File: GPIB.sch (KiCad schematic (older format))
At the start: 24 parts, among them P1 CONN_6, P2 CONN_2, P3 CONN_8, P4 CONN_CENTRONICS_24, SW1 SW_RESET, SW2 SW_BOOTL, U5 STM32F072CBT6, U6 SN75160B, U7 SN75162B

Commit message: Start routing
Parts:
- C10, C11, C6, C7, C8, C9: footprint (none) -> Capacitors_SMD:C_0603_HandSoldering
- D2, D3, D4: footprint (none) -> LEDs:LED-0603
- JP1, P2: footprint (none) -> Pin_Headers:Pin_Header_Straight_1x02
- P1: footprint (none) -> Pin_Headers:Pin_Header_Straight_1x06
- P3: footprint (none) -> Pin_Headers:Pin_Header_Straight_1x08
- P4: footprint (none) -> gpib_conn_male:gpib_conn_male
- R5, R6, R7, R8, R9: footprint (none) -> Resistors_SMD:R_0603_HandSoldering
- SW1, SW2: footprint (none) -> open-project:SW_PUSH_SMD
- U5: footprint LQFP48 -> LQFP:LQFP-48_7x7mm_Pitch0.5mm
- U6: footprint MODULE -> Housings_SOIC:SOIC-20_7.5x12.8mm_Pitch1.27mm
- U7: footprint MODULE -> Housings_SOIC:SOIC-24_7.5x15.4mm_Pitch1.27mm
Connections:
- net GND: now also P4.12 (SHIELD)

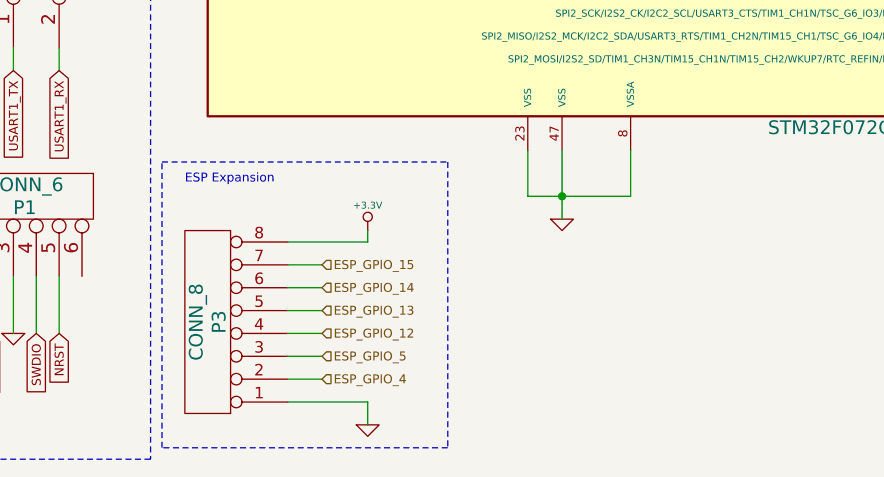
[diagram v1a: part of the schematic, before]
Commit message: Need to swap gpib line driver buses on stm32
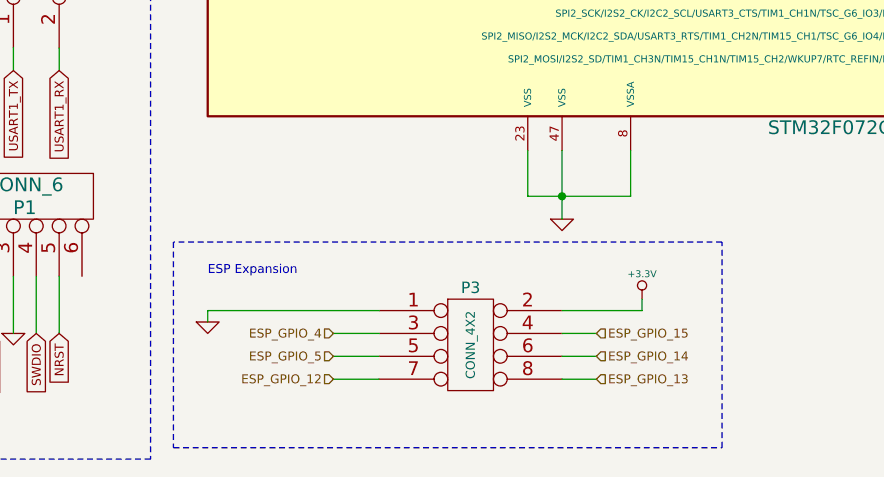
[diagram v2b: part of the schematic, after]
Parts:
- removed P3: CONN_8, Pin_Headers:Pin_Header_Straight_1x08, symbol CONN_8
- added P3: CONN_4X2, Pin_Headers:Pin_Header_Straight_2x04, symbol CONN_4X2
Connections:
- net +3.3V: now also P3.2
- net ESP_GPIO_12: now also P3.7
- net ESP_GPIO_13: now also P3.8
- net ESP_GPIO_14: now also P3.6
- net ESP_GPIO_15: now also P3.4
- net ESP_GPIO_4: now also P3.3
- net ESP_GPIO_5: now also P3.5
- net GND: now also P3.1
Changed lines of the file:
@@
 $EndComp
 $Comp
-L +3.3V #PWR44
+L +3.3V #PWR030
 U 1 1 5567B18B
 P 7200 1550
-F 0 "#PWR44" H 7200 1510 30  0001 C CNN
+F 0 "#PWR030" H 7200 1510 30  0001 C CNN
 F 1 "+3.3V" H 7200 1660 30  0000 C CNN
 F 2 "" H 7200 1550 60  0000 C CNN
@@
 	7750 3000 7750 2500
 $Comp
-L +5V #PWR48
+L +5V #PWR031
 U 1 1 5567BD37
 P 7750 2500
-F 0 "#PWR48" H 7750 2590 20  0001 C CNN
+F 0 "#PWR031" H 7750 2590 20  0001 C CNN
 F 1 "+5V" H 7750 2590 30  0000 C CNN
 F 2 "" H 7750 2500 60  0000 C CNN
@@
 $EndComp
 $Comp
-L +5V #PWR49
+L +5V #PWR032
 U 1 1 5567BE69
 P 7750 4150
-F 0 "#PWR49" H 7750 4240 20  0001 C CNN
+F 0 "#PWR032" H 7750 4240 20  0001 C CNN
 F 1 "+5V" H 7750 4240 30  0000 C CNN
 F 2 "" H 7750 4150 60  0000 C CNN
@@
 	9400 3900 9400 4050
 $Comp
-L GND #PWR52
+L GND #PWR033
 U 1 1 5567BFB4
 P 9400 4050
-F 0 "#PWR52" H 9400 4050 30  0001 C CNN
+F 0 "#PWR033" H 9400 4050 30  0001 C CNN
 F 1 "GND" H 9400 3980 30  0001 C CNN
 F 2 "" H 9400 4050 60  0000 C CNN
@@
 $EndComp
 $Comp
-L GND #PWR50
+L GND #PWR034
 U 1 1 5567BFE0
 P 9250 5900
-F 0 "#PWR50" H 9250 5900 30  0001 C CNN
+F 0 "#PWR034" H 9250 5900 30  0001 C CNN
 F 1 "GND" H 9250 5830 30  0001 C CNN
 F 2 "" H 9250 5900 60  0000 C CNN
@@
 Connection ~ 10750 1650
 $Comp
-L GND #PWR53
+L GND #PWR035
 U 1 1 5567D3C6
 P 10750 1950
-F 0 "#PWR53" H 10750 1950 30  0001 C CNN
+F 0 "#PWR035" H 10750 1950 30  0001 C CNN
 F 1 "GND" H 10750 1880 30  0001 C CNN
 F 2 "" H 10750 1950 60  0000 C CNN
@@
 Connection ~ 9300 1850
 $Comp
-L GND #PWR51
+L GND #PWR036
 U 1 1 5567D5D2
 P 9300 1950
-F 0 "#PWR51" H 9300 1950 30  0001 C CNN
+F 0 "#PWR036" H 9300 1950 30  0001 C CNN
 F 1 "GND" H 9300 1880 30  0001 C CNN
 F 2 "" H 9300 1950 60  0000 C CNN
@@
 	9250 4750 9400 4750
 $Comp
-L GND #PWR47
+L GND #PWR037
 U 1 1 556803AF
 P 7500 4600
-F 0 "#PWR47" H 7500 4600 30  0001 C CNN
+F 0 "#PWR037" H 7500 4600 30  0001 C CNN
 F 1 "GND" H 7500 4530 30  0001 C CNN
 F 2 "" H 7500 4600 60  0000 C CNN
@@
 $EndComp
 $Comp
-L GND #PWR46
+L GND #PWR038
 U 1 1 55680412
 P 7500 2950
-F 0 "#PWR46" H 7500 2950 30  0001 C CNN
+F 0 "#PWR038" H 7500 2950 30  0001 C CNN
 F 1 "GND" H 7500 2880 30  0001 C CNN
 F 2 "" H 7500 2950 60  0000 C CNN
@@
 	7500 4150 7750 4150
 $Comp
-L GND #PWR45
+L GND #PWR039
 U 1 1 5569A4CE
 P 7200 1900
-F 0 "#PWR45" H 7200 1900 30  0001 C CNN
+F 0 "#PWR039" H 7200 1900 30  0001 C CNN
 F 1 "GND" H 7200 1830 30  0001 C CNN
 F 2 "" H 7200 1900 60  0000 C CNN
@@
 	5700 1850 5500 1850
 $Comp
-L +3.3V #PWR29
+L +3.3V #PWR040
 U 1 1 5569A6B6
 P 1100 900
-F 0 "#PWR29" H 1100 860 30  0001 C CNN
+F 0 "#PWR040" H 1100 860 30  0001 C CNN
 F 1 "+3.3V" H 1100 1010 30  0000 C CNN
 F 2 "" H 1100 900 60  0000 C CNN
@@
 $EndComp
 $Comp
-L GND #PWR34
+L GND #PWR041
 U 1 1 5569A6D7
 P 1800 1500
-F 0 "#PWR34" H 1800 1500 30  0001 C CNN
+F 0 "#PWR041" H 1800 1500 30  0001 C CNN
 F 1 "GND" H 1800 1430 30  0001 C CNN
 F 2 "" H 1800 1500 60  0000 C CNN
@@
 $EndComp
 $Comp
-L +3.3V #PWR31
+L +3.3V #PWR042
 U 1 1 5569BF9D
 P 1300 2700
-F 0 "#PWR31" H 1300 2660 30  0001 C CNN
+F 0 "#PWR042" H 1300 2660 30  0001 C CNN
 F 1 "+3.3V" H 1300 2810 30  0000 C CNN
 F 2 "" H 1300 2700 60  0000 C CNN
@@
 Wire Wire Line
 	1300 3200 1850 3200
-Text HLabel 2500 7350 2    39   Input ~ 0
+Text HLabel 2550 7150 0    39   Input ~ 0
 ESP_GPIO_4
-Text HLabel 2500 7250 2    39   Input ~ 0
+Text HLabel 2550 7250 0    39   Input ~ 0
 ESP_GPIO_5
 Wire Wire Line
@@
 $EndComp
 $Comp
-L +3.3V #PWR38
+L +3.3V #PWR043
 U 1 1 556A233C
 P 3000 1350
-F 0 "#PWR38" H 3000 1310 30  0001 C CNN
+F 0 "#PWR043" H 3000 1310 30  0001 C CNN
 F 1 "+3.3V" H 3000 1460 30  0000 C CNN
 F 2 "" H 3000 1350 60  0000 C CNN
@@
 	3000 1450 3000 1350
 $Comp
-L GND #PWR35
+L GND #PWR044
 U 1 1 556A24E8
 P 2300 2000
-F 0 "#PWR35" H 2300 2000 30  0001 C CNN
+F 0 "#PWR044" H 2300 2000 30  0001 C CNN
 F 1 "GND" H 2300 1930 30  0001 C CNN
 F 2 "" H 2300 2000 60  0000 C CNN
@@
 Bootloader mode button
 $Comp
-L +3.3V #PWR39
+L +3.3V #PWR045
 U 1 1 556A2965
 P 3550 2000
-F 0 "#PWR39" H 3550 1960 30  0001 C CNN
+F 0 "#PWR045" H 3550 1960 30  0001 C CNN
 F 1 "+3.3V" H 3550 2110 30  0000 C CNN
 F 2 "" H 3550 2000 60  0000 C CNN
@@
 Connection ~ 3550 2150
 $Comp
-L +3.3V #PWR41
+L +3.3V #PWR046
 U 1 1 556A2C71
 P 5550 6200
-F 0 "#PWR41" H 5550 6160 30  0001 C CNN
+F 0 "#PWR046" H 5550 6160 30  0001 C CNN
 F 1 "+3.3V" H 5550 6310 30  0000 C CNN
 F 2 "" H 5550 6200 60  0000 C CNN
@@
 $EndComp
 $Comp
-L GND #PWR42
+L GND #PWR047
 U 1 1 556A2E45
 P 5550 6700
-F 0 "#PWR42" H 5550 6700 30  0001 C CNN
+F 0 "#PWR047" H 5550 6700 30  0001 C CNN
 F 1 "GND" H 5550 6630 30  0001 C CNN
 F 2 "" H 5550 6700 60  0000 C CNN
@@
 Connection ~ 5800 6200
 $Comp
-L GND #PWR40
+L GND #PWR048
 U 1 1 556A335E
 P 3550 6650
-F 0 "#PWR40" H 3550 6650 30  0001 C CNN
+F 0 "#PWR048" H 3550 6650 30  0001 C CNN
 F 1 "GND" H 3550 6580 30  0001 C CNN
 F 2 "" H 3550 6650 60  0000 C CNN
@@
 	5250 3750 5400 3750
 $Comp
-L GND #PWR30
+L GND #PWR049
 U 1 1 556A686C
 P 1150 7150
-F 0 "#PWR30" H 1150 7150 30  0001 C CNN
+F 0 "#PWR049" H 1150 7150 30  0001 C CNN
 F 1 "GND" H 1150 7080 30  0001 C CNN
 F 2 "" H 1150 7150 60  0000 C CNN
@@
 $EndComp
 $Comp
-L +3.3V #PWR28
+L +3.3V #PWR050
 U 1 1 556A68A8
 P 950 7150
-F 0 "#PWR28" H 950 7110 30  0001 C CNN
+F 0 "#PWR050" H 950 7110 30  0001 C CNN
 F 1 "+3.3V" H 950 7260 30  0000 C CNN
 F 2 "" H 950 7150 60  0000 C CNN
@@
 $EndComp
 $Comp
-L GND #PWR43
+L GND #PWR051
 U 1 1 556AE58B
 P 7200 1250
-F 0 "#PWR43" H 7200 1250 30  0001 C CNN
+F 0 "#PWR051" H 7200 1250 30  0001 C CNN
 F 1 "GND" H 7200 1180 30  0001 C CNN
 F 2 "" H 7200 1250 60  0000 C CNN
@@
 Wire Wire Line
 	5250 5750 5500 5750
-Text HLabel 2500 7150 2    39   Input ~ 0
+Text HLabel 2550 7350 0    39   Input ~ 0
 ESP_GPIO_12
-Text HLabel 2500 7050 2    39   Input ~ 0
+Text HLabel 3700 7350 2    39   Input ~ 0
 ESP_GPIO_13
-Text HLabel 2500 6950 2    39   Input ~ 0
+Text HLabel 3700 7250 2    39   Input ~ 0
 ESP_GPIO_14
-Text HLabel 2500 6850 2    39   Input ~ 0
+Text HLabel 3700 7150 2    39   Input ~ 0
 ESP_GPIO_15
 Text HLabel 5550 5450 2    39   Input ~ 0
@@
 	1850 4750 1700 4750
 $Comp
-L GND #PWR32
+L GND #PWR052
 U 1 1 556BAB4A
 P 1400 4800
-F 0 "#PWR32" H 1400 4800 30  0001 C CNN
+F 0 "#PWR052" H 1400 4800 30  0001 C CNN
 F 1 "GND" H 1400 4730 30  0001 C CNN
 F 2 "" H 1400 4800 60  0000 C CNN
@@
 $EndComp
 $Comp
-L +3.3V #PWR33
+L +3.3V #PWR053
 U 1 1 556BADA7
 P 1700 4750
-F 0 "#PWR33" H 1700 4710 30  0001 C CNN
+F 0 "#PWR053" H 1700 4710 30  0001 C CNN
 F 1 "+3.3V" H 1700 4860 30  0000 C CNN
 F 2 "" H 1700 4750 60  0000 C CNN
@@
 Wire Wire Line
 	1400 4650 1400 4800
-$Comp
-L CONN_8 P3
-U 1 1 556BB559
+Wire Wire Line
+	2550 7350 2750 7350
+Wire Wire Line
+	3550 7350 3700 7350
+Wire Wire Line
+	3550 7250 3700 7250
+Wire Wire Line
+	3550 7150 3700 7150
+$Comp
+L GND #PWR054
+U 1 1 556BBE46
 P 2000 7100
-F 0 "P3" V 1950 7100 60  0000 C CNN
-F 1 "CONN_8" V 2050 7100 60  0000 C CNN
-F 2 "Pin_Headers:Pin_Header_Straight_1x08" H 2000 7100 60  0001 C CNN
+F 0 "#PWR054" H 2000 7100 30  0001 C CNN
+F 1 "GND" H 2000 7030 30  0001 C CNN
+F 2 "" H 2000 7100 60  0000 C CNN
 F 3 "" H 2000 7100 60  0000 C CNN
 	1    2000 7100
-	-1   0    0    1
-$EndComp
-Wire Wire Line
-	2350 7450 2700 7450
-Wire Wire Line
-	2350 7350 2500 7350
-Wire Wire Line
-	2350 7250 2500 7250
-Wire Wire Line
-	2350 7150 2500 7150
-Wire Wire Line
-	2350 7050 2500 7050
-Wire Wire Line
-	2350 6950 2500 6950
-Wire Wire Line
-	2350 6850 2500 6850
-$Comp
-L GND #PWR37
-U 1 1 556BBE46
-P 2700 7550
-F 0 "#PWR37" H 2700 7550 30  0001 C CNN
-F 1 "GND" H 2700 7480 30  0001 C CNN
-F 2 "" H 2700 7550 60  0000 C CNN
-F 3 "" H 2700 7550 60  0000 C CNN
-	1    2700 7550
-	1    0    0    -1
-$EndComp
-$Comp
-L +3.3V #PWR36
+	1    0    0    -1
+$EndComp
+$Comp
+L +3.3V #PWR055
 U 1 1 556BBE7F
-P 2700 6700
-F 0 "#PWR36" H 2700 6660 30  0001 C CNN
-F 1 "+3.3V" H 2700 6810 30  0000 C CNN
-F 2 "" H 2700 6700 60  0000 C CNN
-F 3 "" H 2700 6700 60  0000 C CNN
-	1    2700 6700
-	1    0    0    -1
-$EndComp
-Wire Wire Line
-	2350 6750 2700 6750
-Wire Wire Line
-	2700 6750 2700 6700
-Wire Wire Line
-	2700 7450 2700 7550
-Wire Notes Line
-	1800 6400 3050 6400
-Wire Notes Line
-	3050 6400 3050 7650
-Wire Notes Line
-	3050 7650 1800 7650
-Wire Notes Line
-	1800 7650 1800 6400
-Text Notes 1900 6500 0    39   ~ 0
+P 3900 7000
+F 0 "#PWR055" H 3900 6960 30  0001 C CNN
+F 1 "+3.3V" H 3900 7110 30  0000 C CNN
+F 2 "" H 3900 7000 60  0000 C CNN
+F 3 "" H 3900 7000 60  0000 C CNN
+	1    3900 7000
+	1    0    0    -1
+$EndComp
+Wire Wire Line
+	3550 7050 3900 7050
+Wire Wire Line
+	3900 7050 3900 7000
+Text Notes 2000 6900 0    39   ~ 0
 ESP Expansion\n
 Text GLabel 1350 7150 3    39   Input ~ 0
@@
 Wire Wire Line
 	11150 1250 11150 1650
+$Comp
+L CONN_4X2 P3
+U 1 1 556C4C30
+P 3150 7200
+F 0 "P3" H 3150 7450 50  0000 C CNN
+F 1 "CONN_4X2" V 3150 7200 40  0000 C CNN
+F 2 "Pin_Headers:Pin_Header_Straight_2x04" H 3150 7200 60  0001 C CNN
+F 3 "" H 3150 7200 60  0000 C CNN
+	1    3150 7200
+	1    0    0    -1
+$EndComp
+Wire Wire Line
+	2550 7250 2750 7250
+Wire Wire Line
+	2550 7150 2750 7150
+Wire Wire Line
+	2750 7050 2000 7050
+Wire Wire Line
+	2000 7050 2000 7100
+Wire Notes Line
+	1850 7650 4250 7650
+Wire Notes Line
+	4250 7650 4250 6750
+Wire Notes Line
+	4250 6750 1850 6750
+Wire Notes Line
+	1850 6750 1850 7650
 $EndSCHEMATC
